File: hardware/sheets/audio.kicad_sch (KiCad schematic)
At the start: 18 parts, among them J2 LineOut_TRS, U1 MCP6002

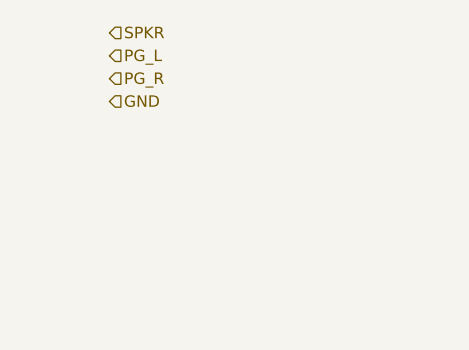
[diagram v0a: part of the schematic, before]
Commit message: ERC cleanup: NC flags on unused pins, anchored interface labels
KiCad 10 ERC drops from 366 to 16 violations, all noise:

- NC flags on the 36 genuinely unused pins (cpu_core '138/'161 spares,
  Supervisor RP2040 unused GPIO, Core2350B GPIO44-47, rtc '138 spares).
- emit_interface anchors every hier label on a stub wire ending in a
  same-name local label -- connectivity unchanged (still by name;
  netlist spans verified), but nothing dangles.
- Interface honesty: cpu_core drops AEN/IOCHRDY from PINS (both live on
  bus_mcu; nothing here touched them), bus_mcu drops PRIV_COUNTER (the
  counter chain is on-sheet, CNT_* never crosses).
- Remaining 6 label_dangling are root IRQ9-13/15: single-sheet by
  design (soft-PIC pull-ups await future 16-bit sources); kept in PINS
  as the AT-style contract.

Co-Authored-By: Claude Fable 5 <noreply@anthropic.com>
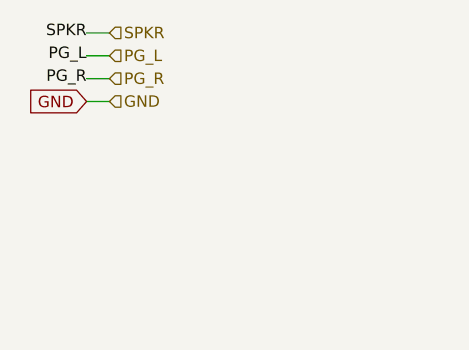
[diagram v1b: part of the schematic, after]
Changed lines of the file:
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@@
 		(company "Andrew C. Young")
+	)
+	(wire
+		(pts
+			(xy 22.86 25.4)
+			(xy 25.4 25.4)
+		)
+		(stroke
+			(width 0)
+			(type default)
+		)
+	)
+	(label "SPKR"
+		(at 22.86 25.4 180)
+		(effects
+			(font
+				(size 1.27 1.27)
+			)
+			(justify right)
+		)
 	)
 	(hierarchical_label "SPKR"
@@
 		)
 	)
+	(wire
+		(pts
+			(xy 22.86 27.94)
+			(xy 25.4 27.94)
+		)
+		(stroke
+			(width 0)
+			(type default)
+		)
+	)
+	(label "PG_L"
+		(at 22.86 27.94 180)
+		(effects
+			(font
+				(size 1.27 1.27)
+			)
+			(justify right)
+		)
+	)
 	(hierarchical_label "PG_L"
 		(shape input)
@@
 		)
 	)
+	(wire
+		(pts
+			(xy 22.86 30.48)
+			(xy 25.4 30.48)
+		)
+		(stroke
+			(width 0)
+			(type default)
+		)
+	)
+	(label "PG_R"
+		(at 22.86 30.48 180)
+		(effects
+			(font
+				(size 1.27 1.27)
+			)
+			(justify right)
+		)
+	)
 	(hierarchical_label "PG_R"
 		(shape input)
@@
 				(size 1.27 1.27)
 			)
+		)
+	)
+	(wire
+		(pts
+			(xy 22.86 33.02)
+			(xy 25.4 33.02)
+		)
+		(stroke
+			(width 0)
+			(type default)
+		)
+	)
+	(global_label "GND"
+		(shape input)
+		(at 22.86 33.02 180)
+		(effects
+			(font
+				(size 1.27 1.27)
+			)
+			(justify right)
 		)
 	)
@@
 		(instances
 			(project "mini-xt"
-				(path "/26736c46-8b40-5460-874f-03596d17270c/4d185cde-1239-5609-9fdc-bfd3b5da75e8"
+				(path "/26736c46-8b40-5460-874f-03596d17270c/2bb3f33d-e1c7-5155-9107-469b56751757"
 					(reference "R1101")
 					(unit 1)
@@
 		(instances
 			(project "mini-xt"
-				(path "/26736c46-8b40-5460-874f-03596d17270c/4d185cde-1239-5609-9fdc-bfd3b5da75e8"
+				(path "/26736c46-8b40-5460-874f-03596d17270c/2bb3f33d-e1c7-5155-9107-469b56751757"
 					(reference "R1102")
 					(unit 1)
@@
 		(instances
 			(project "mini-xt"
-				(path "/26736c46-8b40-5460-874f-03596d17270c/4d185cde-1239-5609-9fdc-bfd3b5da75e8"
+				(path "/26736c46-8b40-5460-874f-03596d17270c/2bb3f33d-e1c7-5155-9107-469b56751757"
 					(reference "C1101")
 					(unit 1)
@@
 		(instances
 			(project "mini-xt"
-				(path "/26736c46-8b40-5460-874f-03596d17270c/4d185cde-1239-5609-9fdc-bfd3b5da75e8"
+				(path "/26736c46-8b40-5460-874f-03596d17270c/2bb3f33d-e1c7-5155-9107-469b56751757"
 					(reference "R1103")
 					(unit 1)
@@
 		(instances
 			(project "mini-xt"
-				(path "/26736c46-8b40-5460-874f-03596d17270c/4d185cde-1239-5609-9fdc-bfd3b5da75e8"
+				(path "/26736c46-8b40-5460-874f-03596d17270c/2bb3f33d-e1c7-5155-9107-469b56751757"
 					(reference "C1102")
 					(unit 1)
@@
 		(instances
 			(project "mini-xt"
-				(path "/26736c46-8b40-5460-874f-03596d17270c/4d185cde-1239-5609-9fdc-bfd3b5da75e8"
+				(path "/26736c46-8b40-5460-874f-03596d17270c/2bb3f33d-e1c7-5155-9107-469b56751757"
 					(reference "C1103")
 					(unit 1)
@@
 		(instances
 			(project "mini-xt"
-				(path "/26736c46-8b40-5460-874f-03596d17270c/4d185cde-1239-5609-9fdc-bfd3b5da75e8"
+				(path "/26736c46-8b40-5460-874f-03596d17270c/2bb3f33d-e1c7-5155-9107-469b56751757"
 					(reference "C1104")
 					(unit 1)
@@
 		(instances
 			(project "mini-xt"
-				(path "/26736c46-8b40-5460-874f-03596d17270c/4d185cde-1239-5609-9fdc-bfd3b5da75e8"
+				(path "/26736c46-8b40-5460-874f-03596d17270c/2bb3f33d-e1c7-5155-9107-469b56751757"
 					(reference "C1105")
 					(unit 1)
@@
 		(instances
 			(project "mini-xt"
-				(path "/26736c46-8b40-5460-874f-03596d17270c/4d185cde-1239-5609-9fdc-bfd3b5da75e8"
+				(path "/26736c46-8b40-5460-874f-03596d17270c/2bb3f33d-e1c7-5155-9107-469b56751757"
 					(reference "U1101")
 					(unit 1)
@@
 		(instances
 			(project "mini-xt"
-				(path "/26736c46-8b40-5460-874f-03596d17270c/4d185cde-1239-5609-9fdc-bfd3b5da75e8"
+				(path "/26736c46-8b40-5460-874f-03596d17270c/2bb3f33d-e1c7-5155-9107-469b56751757"
 					(reference "C1106")
 					(unit 1)
@@
 		(instances
 			(project "mini-xt"
-				(path "/26736c46-8b40-5460-874f-03596d17270c/4d185cde-1239-5609-9fdc-bfd3b5da75e8"
+				(path "/26736c46-8b40-5460-874f-03596d17270c/2bb3f33d-e1c7-5155-9107-469b56751757"
 					(reference "R1104")
 					(unit 1)
@@
 		(instances
 			(project "mini-xt"
-				(path "/26736c46-8b40-5460-874f-03596d17270c/4d185cde-1239-5609-9fdc-bfd3b5da75e8"
+				(path "/26736c46-8b40-5460-874f-03596d17270c/2bb3f33d-e1c7-5155-9107-469b56751757"
 					(reference "R1105")
 					(unit 1)
@@
 		(instances
 			(project "mini-xt"
-				(path "/26736c46-8b40-5460-874f-03596d17270c/4d185cde-1239-5609-9fdc-bfd3b5da75e8"
+				(path "/26736c46-8b40-5460-874f-03596d17270c/2bb3f33d-e1c7-5155-9107-469b56751757"
 					(reference "R1110")
 					(unit 1)
@@
 		(instances
 			(project "mini-xt"
-				(path "/26736c46-8b40-5460-874f-03596d17270c/4d185cde-1239-5609-9fdc-bfd3b5da75e8"
+				(path "/26736c46-8b40-5460-874f-03596d17270c/2bb3f33d-e1c7-5155-9107-469b56751757"
 					(reference "R1106")
 					(unit 1)
@@
 		(instances
 			(project "mini-xt"
-				(path "/26736c46-8b40-5460-874f-03596d17270c/4d185cde-1239-5609-9fdc-bfd3b5da75e8"
+				(path "/26736c46-8b40-5460-874f-03596d17270c/2bb3f33d-e1c7-5155-9107-469b56751757"
 					(reference "R1107")
 					(unit 1)
@@
 		(instances
 			(project "mini-xt"
-				(path "/26736c46-8b40-5460-874f-03596d17270c/4d185cde-1239-5609-9fdc-bfd3b5da75e8"
+				(path "/26736c46-8b40-5460-874f-03596d17270c/2bb3f33d-e1c7-5155-9107-469b56751757"
 					(reference "C1107")
 					(unit 1)
@@
 		(instances
 			(project "mini-xt"
-				(path "/26736c46-8b40-5460-874f-03596d17270c/4d185cde-1239-5609-9fdc-bfd3b5da75e8"
+				(path "/26736c46-8b40-5460-874f-03596d17270c/2bb3f33d-e1c7-5155-9107-469b56751757"
 					(reference "R1108")
 					(unit 1)
@@
 		(instances
 			(project "mini-xt"
-				(path "/26736c46-8b40-5460-874f-03596d17270c/4d185cde-1239-5609-9fdc-bfd3b5da75e8"
+				(path "/26736c46-8b40-5460-874f-03596d17270c/2bb3f33d-e1c7-5155-9107-469b56751757"
 					(reference "J1102")
 					(unit 1)

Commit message: Parts: footprints for all components, close 6 LCSC map gaps, check_parts.py
- mxsch.py emits the Footprint property from component props (was
  hard-coded empty); parts.py entries now carry a verified KiCad
  footprint, applied at build time alongside the LCSC number.
- Map keys fixed to match placed values: USB_PROG, SS34, LED (PicoGUS),
  APS6404L, CB3T3257/45 -- every combo across all sheets + cards now
  resolves (130 combos, 455 netlist components, all with footprints).
- Package corrections from JLC DB re-check: RTL8019AS is QFP-100 14x20
  P0.65 (not TQFP); C2897411 female header is a 2x10 strip -- fine for
  Core2350B, Pico needs 2x 1x20 (noted in jlcpcb-sourcing.md).
- 10 mini-xt:* placeholder footprints mark parts whose land pattern is
  authored at layout from the EasyEDA data (CH224K, magnetics, RJ45,
  HDMI, CF socket, ISA slot, switches, Core2350B PGA).
- New tools/check_parts.py: fails on unmapped combos, missing fp
  fields, or footprints absent from the installed KiCad libs.

Co-Authored-By: Claude Fable 5 <noreply@anthropic.com>
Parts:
- C1, C7: footprint (none) -> Capacitor_SMD:C_0805_2012Metric
- C2, C3, C4, C5, C6: footprint (none) -> Capacitor_SMD:C_0603_1608Metric
- J2: footprint (none) -> Connector_PinHeader_2.54mm:PinHeader_1x03_P2.54mm_Vertical
- R1, R10, R2, R3, R4, R5, R6, R7, R8: footprint (none) -> Resistor_SMD:R_0603_1608Metric
- U1: footprint (none) -> Package_SO:SOIC-8_3.9x4.9mm_P1.27mm
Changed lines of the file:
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@@
 			)
 		)
-		(property "Footprint" ""
+		(property "Footprint" "Resistor_SMD:R_0603_1608Metric"
 			(at 50.8 76.2 0)
 			(effects
@@
 			)
 		)
-		(property "Footprint" ""
+		(property "Footprint" "Resistor_SMD:R_0603_1608Metric"
 			(at 50.8 109.22 0)
 			(effects
@@
 			)
 		)
-		(property "Footprint" ""
+		(property "Footprint" "Capacitor_SMD:C_0805_2012Metric"
 			(at 76.2 109.22 0)
 			(effects
@@
 			)
 		)
-		(property "Footprint" ""
+		(property "Footprint" "Resistor_SMD:R_0603_1608Metric"
 			(at 50.8 165.1 0)
 			(effects
@@
 			)
 		)
-		(property "Footprint" ""
+		(property "Footprint" "Capacitor_SMD:C_0603_1608Metric"
 			(at 76.2 198.12 0)
 			(effects
@@
 			)
 		)
-		(property "Footprint" ""
+		(property "Footprint" "Capacitor_SMD:C_0603_1608Metric"
 			(at 101.6 165.1 0)
 			(effects
@@
 			)
 		)
-		(property "Footprint" ""
+		(property "Footprint" "Capacitor_SMD:C_0603_1608Metric"
 			(at 101.6 215.9 0)
 			(effects
@@
 			)
 		)
-		(property "Footprint" ""
+		(property "Footprint" "Capacitor_SMD:C_0603_1608Metric"
 			(at 101.6 241.3 0)
 			(effects
@@
 			)
 		)
-		(property "Footprint" ""
+		(property "Footprint" "Package_SO:SOIC-8_3.9x4.9mm_P1.27mm"
 			(at 177.8 152.4 0)
 			(effects
@@
 			)
 		)
-		(property "Footprint" ""
+		(property "Footprint" "Capacitor_SMD:C_0603_1608Metric"
 			(at 203.2 101.6 0)
 			(effects
@@
 			)
 		)
-		(property "Footprint" ""
+		(property "Footprint" "Resistor_SMD:R_0603_1608Metric"
 			(at 127 127 0)
 			(effects
@@
 			)
 		)
-		(property "Footprint" ""
+		(property "Footprint" "Resistor_SMD:R_0603_1608Metric"
 			(at 152.4 127 0)
 			(effects
@@
 			)
 		)
-		(property "Footprint" ""
+		(property "Footprint" "Resistor_SMD:R_0603_1608Metric"
 			(at 152.4 177.8 0)
 			(effects
@@
 			)
 		)
-		(property "Footprint" ""
+		(property "Footprint" "Resistor_SMD:R_0603_1608Metric"
 			(at 203.2 127 0)
 			(effects
@@
 			)
 		)
-		(property "Footprint" ""
+		(property "Footprint" "Resistor_SMD:R_0603_1608Metric"
 			(at 241.3 127 0)
 			(effects
@@
 			)
 		)
-		(property "Footprint" ""
+		(property "Footprint" "Capacitor_SMD:C_0805_2012Metric"
 			(at 228.6 127 0)
 			(effects
@@
 			)
 		)
-		(property "Footprint" ""
+		(property "Footprint" "Resistor_SMD:R_0603_1608Metric"
 			(at 254 101.6 0)
 			(effects
@@
 			)
 		)
-		(property "Footprint" ""
+		(property "Footprint" "Connector_PinHeader_2.54mm:PinHeader_1x03_P2.54mm_Vertical"
 			(at 266.7 152.4 0)
 			(effects
